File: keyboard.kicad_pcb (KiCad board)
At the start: 2 copper layers, 285 x 94.6 mm, 398 parts, among them IC1 ATMEGA32U4, J1 MINI, J2 MICRO, P1 CONN_1, P10 CONN_1, P11 CONN_1, P12 CONN_1, P13 CONN_1, P14 CONN_1, P15 CONN_1, P16 CONN_1, P17 CONN_1, P18 CONN_1, P19 CONN_1, P2 CONN_1, P20 CONN_1, P21 CONN_1, P22 CONN_1, P23 CONN_1, P24 CONN_1, P25 CONN_1, P26 CONN_1, P27 CONN_1, P28 CONN_1, P29 CONN_1, P3 CONN_1, P30 CONN_1, P31 CONN_1, P32 CONN_1, P33 CONN_1, P34 CONN_1, P35 CONN_1, P36 CONN_1, P37 CONN_1, P38 CONN_1, P39 CONN_1, P4 CONN_1, P40 CONN_1, P41 CONN_1, P42 CONN_1, P5 CONN_1, P6 CONN_1, P7 CONN_1, P8 CONN_1, P9 CONN_1, Q1 MOSFET_P, X1 CRYSTAL

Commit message: 完成
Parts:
- removed D01, D02, D03, D04, D05, D06, D07, D08, D09: 1N4148, SM0805D
- removed DB10, DB101, DB102, DB11, DB14, DB15, DB151, DB16, DB17, DB19, DB2, DB21, DB22, DB23, DB24, DB26, DB27, DB28, DB29, DB30, DB301, DB302, DB31, DB32, DB33, DB34, DB36, DB37, DB38, DB39, DB4, DB41, DB42, DB43, DB44, DB46, DB47, DB48, DB49, DB4_1, DB5, DB50, DB51, DB52, DB53, DB54, DB55, DB551, DB56, DB57, DB58, DB59, DB5_1, DB6, DB61, DB62, DB63, DB66, DB661, DB67, DB68, DB681, DB682, DB69, DB7, DB9, DF10, DF11, DF20, DF201, DF21, DF211, DF22, DF221, DF23, DF231, DF232, DF3, DW1, DW2, DW3, DW4: LED, MX1A-led
- removed FID (x2): FIDUCIAL, FIDUCIAL
- removed IC1: ATMEGA32U4, TQFP44
- removed J2: MICRO, Connect:USB_Micro-B
- removed JP1, JP2, JP3, JP4, JP5, JP6: JUMPER, Resistors_SMD:R_0201
- removed MXWIRE (x9): VAL**, MX1A-wire
- removed P1, P10, P11, P12, P13, P14, P15, P16, P17, P18, P19, P20, P21, P22, P23, P24, P25, P26, P27, P28, P29, P30, P31, P32, P33, P34, P35, P36, P37, P38, P39, P4, P40, P41, P42, P5, P6, P7, P8, P9: CONN_1, pad
- removed Q1: MOSFET_P, TO_SOT_Packages_SMD:SOT-23
- removed R11, R12, R13, R14, R15, R16, R17, R18, R19, R20, R21, R22, R23, R24, R25, R26, R27, R28, R29, R30, R31, R32, R33, R34, R35, R36, R37, R38, R39, R40, R41, R42, R43, R44, R45, R46, R47, R48, R49, R50, R51, R52, R53, R54, R55, R56, R57, R58, R59, R60, R61, R62, R63, R64, RL1, RL2, RL3, RL4, RL5: 300, Resistors_SMD:R_0805
- removed R65: 10k, Resistors_SMD:R_0805
- removed S0: DTSM-6, KSEM31GLFS
- removed S01, S02, S03, S04, S05, S0512, S06, S07, S08, S09: MX1A, MX1A-b
- removed X1: CRYSTAL, Crystals:Crystal_HC49-U_Vertical
- added D1: 1N4148, Diode_SMD:D_0805_2012Metric, B.Cu at (67.5, 81.5)
- added D2: 1N4148, Diode_SMD:D_0805_2012Metric, B.Cu at (68.6, 98.0)
- added D20: LED, MX1A:MX1A-led, F.Cu at (90.5, 73.8)
- added D25: LED, MX1A:MX1A-led, F.Cu at (109.5, 73.8)
- added D3: 1N4148, Diode_SMD:D_0805_2012Metric, B.Cu at (67.9, 117.0)
- added D35: LED, MX1A:MX1A-led, F.Cu at (128.6, 73.8)
- added D4: 1N4148, Diode_SMD:D_0805_2012Metric, B.Cu at (68.2, 136.1)
- added D40: LED, MX1A:MX1A-led, F.Cu at (147.6, 73.8)
- added D45: LED, MX1A:MX1A-led, F.Cu at (166.7, 73.8)
- added D5: 1N4148, Diode_SMD:D_0805_2012Metric, B.Cu at (70.1, 152.7)
- added D6: 1N4148, Diode_SMD:D_0805_2012Metric, B.Cu at (87.0, 81.8)
- added D7: 1N4148, Diode_SMD:D_0805_2012Metric, B.Cu at (94.9, 95.6)
- added D8: 1N4148, Diode_SMD:D_0805_2012Metric, B.Cu at (101.2, 119.9)
- added D9: 1N4148, Diode_SMD:D_0805_2012Metric, B.Cu at (91.4, 133.6)
- added G***: LOGO, custom:Cirno_Ice, B.Cu at (135.9, 149.6)
- added K1: Jumper_NO_Small, Resistor_SMD:R_0805_2012Metric, B.Cu at (157.7, 140.0)
- added S1: MX1A, MX1A:MX1A-simple, F.Cu at (71.4, 73.8)
- added S2: MX1A, MX1A:MX1A-simple, F.Cu at (76.2, 92.9)
- added S3: MX1A, MX1A:MX1A-simple, F.Cu at (73.8, 111.9)
- added S4: MX1A, MX1A:MX1A-simple, F.Cu at (83.3, 131.0)
- added S5: MX1A, MX1A:MX1A-simple, F.Cu at (73.8, 150.0)
- added S512: MX1A, MX1A:MX1A-simple, F.Cu at (76.2, 150.0)
- added S6: MX1A, MX1A:MX1A-simple, F.Cu at (90.5, 73.8)
- added S7: MX1A, MX1A:MX1A-simple, F.Cu at (100.0, 92.9)
- added S8: MX1A, MX1A:MX1A-simple, F.Cu at (104.8, 111.9)
- added S9: MX1A, MX1A:MX1A-simple, F.Cu at (95.2, 131.0)
- added U1: nrf51822-02, custom:nRF51822-02, B.Cu at (211.2, 158.5)
- added U2: TP4057, Package_TO_SOT_SMD:SOT-23-6, B.Cu at (155.6, 152.9)
- added U3: RT9193, Package_TO_SOT_SMD:SOT-23-5, B.Cu at (158.9, 156.7)
- added U4: CH554T, Package_SO:SSOP-20_4.4x6.5mm_P0.65mm, B.Cu at (163.3, 145.8)
- C1: value 22p -> 22nF; footprint SM0805 -> Capacitor_SMD:C_0805_2012Metric
- C2: value 22p -> 1uF; footprint SM0805 -> Capacitor_SMD:C_0805_2012Metric
- C3: value 1u -> 1uF; footprint SM0805 -> Capacitor_SMD:C_0805_2012Metric
- C4: value 100n -> 1uF; footprint SM0805 -> Capacitor_SMD:C_0805_2012Metric
- C5: value 100n -> 22uF; footprint SM0805 -> Capacitor_SMD:C_0805_2012Metric
- C6, C7: value 100n -> 0.1uF; footprint SM0805 -> Capacitor_SMD:C_0805_2012Metric
- C8: value 1u -> 47pF; footprint SM0805 -> Capacitor_SMD:C_0805_2012Metric
- D10, D11, D12, D13, D14, D15, D16, D17, D18, D19, D21, D22, D23, D24, D26, D27, D28, D29, D30, D31, D32, D33, D34, D36, D37, D38, D39, D41, D42, D43, D44, D46, D47, D48, D49, D50, D51, D52, D53, D54, D55, D56, D57, D58, D59, D60, D61, D62, D63, D64, D65, D66, D67, D68, D69, D70: footprint SM0805D -> Diode_SMD:D_0805_2012Metric
- DC1, DC2: footprint MX1A-led -> MX1A:MX1A-led
- DC3: footprint MX1A-ledlock -> MX1A:MX1A-led
- J1: value MINI -> USB_OTG; footprint 67503 -> custom:USB_Micro-B_lowp
- P2: value CONN_1 -> BATT; footprint pad -> Connector_PinHeader_2.54mm:PinHeader_1x02_P2.54mm_Vertical; moved to B.Cu
- P3: value CONN_1 -> SWD; footprint pad -> Connector_PinSocket_2.54mm:PinSocket_1x04_P2.54mm_Vertical; moved to B.Cu
- R1: value 22 -> 1.5K; footprint SM0805 -> Resistor_SMD:R_0805_2012Metric
- R10: value 300 -> 20K; footprint Resistors_SMD:R_0805 -> Resistor_SMD:R_0805_2012Metric
- R2: value 22 -> R; footprint SM0805 -> Resistor_SMD:R_0805_2012Metric
- R3, R5: value 10k -> R; footprint SM0805 -> Resistor_SMD:R_0805_2012Metric
- R4: footprint Resistors_SMD:R_0805 -> Resistor_SMD:R_0805_2012Metric
- R6: value 300 -> 10M; footprint Resistors_SMD:R_0805 -> Resistor_SMD:R_0805_2012Metric
- R7, R9: value 300 -> R; footprint Resistors_SMD:R_0805 -> Resistor_SMD:R_0805_2012Metric
- R8: value 300 -> 2.2M; footprint Resistors_SMD:R_0805 -> Resistor_SMD:R_0805_2012Metric
- S031, S041, S10, S101, S102, S11, S12, S13, S14, S15, S151, S16, S17, S18, S19, S21, S22, S23, S24, S26, S27, S28, S29, S30, S301, S302, S31, S32, S33, S34, S36, S37, S38, S39, S41, S42, S43, S44, S46, S47, S48, S49, S50, S51, S52, S53, S54, S55, S552, S56, S57, S58, S59, S60, S601, S602, S62, S63, S64, S641, S65, S6512, S66, S661, S67, S68, S681, S682, S69, S691, S692, S70, S7012: footprint MX1A-b -> MX1A:MX1A-simple
- moved C8 105.0 mm to (160.0, 140.0), turned to 270 degrees
- moved R1 104.7 mm to (155.6, 149.9), turned to 0 degrees
- moved R9 100.8 mm to (172.7, 71.0)
- moved R6 87.6 mm to (163.1, 153.7), turned to 0 degrees
- moved R10 86.4 mm to (162.3, 140.0), turned to 270 degrees
- moved R3 85.7 mm to (114.0, 70.2), turned to 0 degrees
- moved R5 83.8 mm to (134.0, 70.1), turned to 0 degrees
- moved R8 72.9 mm to (166.8, 151.5)
- moved P2 64.5 mm to (155.3, 156.8), turned to 90 degrees
- moved R7 58.2 mm to (152.7, 70.6)
- moved R4 33.5 mm to (83.6, 106.8), turned to 180 degrees
- moved P3 30.7 mm to (247.8, 153.3)
- moved C5 17.2 mm to (166.8, 153.7), turned to 0 degrees
- moved R2 15.6 mm to (96.2, 71.0), turned to 0 degrees
- moved C7 15.1 mm to (156.5, 146.8), turned to 270 degrees
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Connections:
- net /Matrix/col10 renamed /col10
- net /Matrix/col11 renamed /col11
- net /Matrix/col12 renamed /col12
- net /Matrix/col13 renamed /col13
- net /Matrix/col14 renamed /col14
- net /Matrix/col3 renamed /col3
- net /Matrix/col4 renamed /col4
- net /Matrix/col5 renamed /col5
- net /Matrix/col6 renamed /col6
- net /Matrix/col7 renamed /col7
- net /Matrix/col9 renamed /col9
- net /Matrix/row1 renamed /row1
- net /Matrix/row2 renamed /row2
- net /Matrix/row3 renamed /row3
- net /Matrix/row4 renamed /row4
- net /Matrix/row5 renamed /row5
- C2 pad 1: Net-(C2-Pad1) -> VCC
- C3 pad 1: Net-(C3-Pad1) -> BATT
- C4 pad 1: VCC -> 3V3
- C5 pad 1: VCC -> ADC1
- C6 pad 1: VCC -> V33
- C8 pad 1: VCC -> Net-(C8-Pad1)
- D10 pad 1: /Matrix/col2 -> /col2
- D36 pad 1: /Matrix/col8 -> /col8
- D37 pad 1: /Matrix/col8 -> /col8
- D38 pad 1: /Matrix/col8 -> /col8
- D39 pad 1: /Matrix/col8 -> /col8
- DC1 pad 1: VCC -> Net-(DC1-Pad1)
- DC1 pad 2: Net-(DC1-Pad2) -> GND
- DC2 pad 1: VCC -> Net-(DC1-Pad1)
- DC2 pad 2: Net-(DC1-Pad2) -> GND
- DC3 pad 1: VCC -> Net-(DC1-Pad1)
- J1 pad 2: Net-(J1-Pad2) -> UD_N
- J1 pad 3: Net-(J1-Pad3) -> UD_P
- J1 pad 4: (no net) -> Net-(J1-Pad4)
- P2 pad 1: VCC -> BATT
- P3 pad 1: /Matrix/col8 -> 3V3
- R1 pad 2: Net-(J1-Pad2) -> GND
- R10 pad 1: Net-(DB11-Pad1) -> Net-(C8-Pad1)
- R10 pad 2: /Leds/lcol3 -> UD_P
- R2 pad 2: Net-(J1-Pad3) -> /led1
- R3 pad 2: GND -> /led2
- R4 pad 1: Net-(DC1-Pad2) -> /caps_led
- R4 pad 2: /Matrix/CAPS_LED -> Net-(DC1-Pad1)
- R5 pad 1: VCC -> Net-(D35-Pad2)
- R5 pad 2: /~RES~ -> /led3
- R6 pad 1: Net-(DB7-Pad1) -> BATT
- R6 pad 2: /Leds/lcol2 -> ADC1
- R7 pad 2: /Leds/lcol2 -> /led4
- R8 pad 1: Net-(DB9-Pad1) -> ADC1
- R8 pad 2: /Leds/lcol2 -> GND
- R9 pad 2: /Leds/lcol2 -> /led5
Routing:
- net /Leds/lrow5: track 597.7 -> 0.00 mm, vias 18 -> 0
- net GND: track 546.1 -> 102.2 mm, vias 34 -> 11
- net /Leds/lrow1: track 385.6 -> 0.00 mm, vias 3 -> 0
- net /Leds/lrow4: track 377.2 -> 0.00 mm, vias 7 -> 0
- net VCC: track 488.3 -> 165.0 mm, vias 10 -> 4
- net /Leds/lrow2: track 322.1 -> 0.00 mm, vias 6 -> 0
- net /Leds/lrow3: track 297.3 -> 0.00 mm, vias 1 -> 0
- net /GPIO2: track 252.2 -> 0.00 mm, vias 6 -> 0
- net /Leds/lcol10: track 242.3 -> 0.00 mm, vias 7 -> 0
- net /GPIO1: track 240.9 -> 0.00 mm, vias 6 -> 0
- net /Leds/lcol14: track 238.1 -> 0.00 mm, vias 1 -> 0
- net /col1: track 0.00 -> 231.5 mm, vias 0 -> 2
- net /~RES~: track 226.3 -> 0.00 mm, vias 9 -> 0
- net /col2: track 0.00 -> 217.6 mm, vias 0 -> 2
- net /GPIO3: track 213.7 -> 0.00 mm, vias 5 -> 0
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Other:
- outline, holes or cut-outs redrawn
- net class DATA added: clearance 0.2032, trace_width 0.3048, via_dia 1, via_drill 0.4
- net class POWER: trace_width 0.508 -> 0.4064
- board text added: "Cirno id: 52846813"
- board text added: "Lot60-BLE Rev.A ©2018 Lotlab"
- board text removed: "0"
- board text removed: "1"
- board text removed: "2"
- board text removed: "3"
- board text removed: "CAPS"
- board text removed: "GPIO"
- board text removed: "ISP"
- board text removed: "JP2"
- board text removed: "JP3"
- board text removed: "JP4"
- board text removed: "MISO SCK RST"
- board text removed: "R1"
- board text removed: "R2"
- board text removed: "R3"
- board text removed: "R4"
- board text removed: "R5"
- board text removed: "Rev. L v1.01c Modify by Lotlab."
- board text removed: "VCC MOSI GND"
- board text removed: "expansion module"

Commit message: 细节修正
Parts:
- moved D69 5.64 mm to (323.4, 136.5)
- moved D32 5.40 mm to (191.8, 100.9)
- moved G*** 0.09 mm to (135.8, 149.5)
- renumbered C6 to C1, C7 to C2, C8 to C3, C2 to C4, C3 to C5, C4 to C6, C5 to C7, C1 to C8, D20 to LED1, D25 to LED2, D35 to LED3, D40 to LED4, D45 to LED5, P3 to P1, R10 to R1, R1 to R2, R6 to R3, R8 to R4, R4 to RL0, R2 to RL1, R3 to RL2, R5 to RL3, R7 to RL4, R9 to RL5, U4 to U2, U2 to U3, U3 to U4
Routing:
- net /col14: track 175.5 -> 187.4 mm
- net /row2: track 334.6 -> 323.0 mm
- net Net-(D64-Pad2): track 45.2 -> 35.9 mm
- net Net-(D69-Pad2): track 30.0 -> 39.2 mm
- net /row1: track 361.6 -> 368.0 mm, vias 0 -> 2
- net /led3: track 155.7 -> 161.9 mm
- net GND: track 102.2 -> 105.6 mm
- net /led5: track 127.6 -> 130.3 mm
- net /led4: track 138.3 -> 139.6 mm
- net ADC1: track 59.9 -> 60.8 mm
- net /caps_led: track 185.1 -> 185.9 mm
- net /row3: track 332.2 -> 331.5 mm
- net /col3: track 198.1 -> 198.8 mm
- net /col8: track 95.5 -> 94.9 mm
- net /col1: track 231.5 -> 231.0 mm
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
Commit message: 元件丢正面
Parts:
- C1, C2, C4, C5, C6, C8, D1, D10, D11, D12, D13, D14, D15, D16, D17, D18, D19, D2, D21, D22, D23, D24, D26, D27, D28, D29, D3, D30, D31, D32, D33, D34, D36, D37, D38, D39, D4, D41, D42, D43, D44, D46, D47, D48, D49, D5, D50, D51, D52, D53, D54, D55, D56, D57, D58, D59, D6, D60, D61, D62, D63, D64, D65, D66, D67, D68, D69, D7, D70, D8, D9, J1, P1, P2, R1, R2, R3, R4, RL0, RL1, RL2, RL3, RL4, RL5, U1, U2, U3, U4: moved to F.Cu
- C3: value 47pF -> NC/47pF; moved to F.Cu
- C7: value 22uF -> 10nF; moved to F.Cu
- moved P1 99.9 mm to (147.8, 153.0), turned to 180 degrees
- moved G*** 90.1 mm to (225.9, 149.1)
- moved P2 59.5 mm to (212.5, 140.5), turned to 270 degrees
- moved U4 55.7 mm to (214.5, 154.7), turned to 180 degrees
- moved C8 52.3 mm to (214.5, 152.0), turned to 0 degrees
- moved R3 52.0 mm to (214.5, 145.9), turned to 180 degrees
- moved C5 52.0 mm to (214.6, 143.9), turned to 180 degrees
- moved C6 48.4 mm to (214.5, 157.3), turned to 0 degrees
- moved C7 47.9 mm to (214.5, 150.0)
- moved R4 47.9 mm to (214.5, 148.0)
- moved C1 33.3 mm to (137.5, 154.4), turned to 180 degrees
- moved U1 32.4 mm to (178.8, 158.1)
- moved R1 31.8 mm to (134.0, 154.4), turned to 0 degrees
- moved C3 30.8 mm to (134.0, 156.4), turned to 0 degrees
- moved U2 27.8 mm to (135.7, 149.2), turned to 270 degrees
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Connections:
- K1 pad 2: VCC -> V33
- U1 pad 10: /col3 -> /col7
- U1 pad 12: /col4 -> /led5
- U1 pad 13: /col5 -> /col6
- U1 pad 14: /col6 -> /led4
- U1 pad 15: /col7 -> /col5
- U1 pad 16: /col8 -> /led3
- U1 pad 17: /col9 -> /col4
- U1 pad 18: /col10 -> /led2
- U1 pad 19: /col11 -> /col3
- U1 pad 20: /col12 -> /led1
- U1 pad 23: /col13 -> /col2
- U1 pad 24: /col14 -> /caps_led
- U1 pad 25: Net-(U1-Pad25) -> /col1
- U1 pad 3: /row5 -> /col14
- U1 pad 32: /led5 -> TXD
- U1 pad 33: /led4 -> RXD
- U1 pad 34: /led3 -> Net-(U1-Pad34)
- U1 pad 35: /led2 -> /row1
- U1 pad 36: /led1 -> /row2
- U1 pad 37: /caps_led -> /row3
- U1 pad 38: Net-(U1-Pad38) -> /row4
- U1 pad 39: TXD -> /row5
- U1 pad 4: /row4 -> /col13
- U1 pad 40: RXD -> Net-(U1-Pad40)
- U1 pad 5: /row3 -> /col12
- U1 pad 6: /row2 -> /col11
- U1 pad 7: /row1 -> /col10
- U1 pad 8: /col1 -> /col9
- U1 pad 9: /col2 -> /col8
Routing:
- net BATT: track 15.9 -> 102.8 mm, vias 0 -> 3
- net /caps_led: track 185.9 -> 99.5 mm
- net /col6: track 158.6 -> 79.4 mm, vias 2 -> 0
- net /led3: track 161.9 -> 87.0 mm
- net /row1: track 368.0 -> 438.6 mm, vias 2 -> 4
- net /led2: track 181.2 -> 111.7 mm
- net /led1: track 198.1 -> 128.8 mm
- net /col2: track 218.0 -> 157.2 mm
- net /col3: track 198.8 -> 143.2 mm
- net /col13: track 158.1 -> 213.6 mm
- net /col1: track 231.0 -> 176.0 mm
- net /col4: track 162.8 -> 108.9 mm
- net /col5: track 145.3 -> 92.2 mm, vias 2 -> 0
- net /led5: track 130.3 -> 77.9 mm, vias 2 -> 0
- net /led4: track 139.6 -> 88.2 mm
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
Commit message: 修改
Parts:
- removed C8: 22nF, Capacitor_SMD:C_0805_2012Metric
- MXST (x15): footprint MXST -> MX1A:MXST
- U4: value RT9193 -> XC6206P30; footprint Package_TO_SOT_SMD:SOT-23-5 -> Package_TO_SOT_SMD:SOT-23
- moved U4 1.91 mm to (214.5, 152.8), turned to 0 degrees
- moved C6 1.72 mm to (214.5, 155.6)
- moved G*** 1.27 mm to (225.9, 150.4)
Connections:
- U4 pad 1: BATT -> GND
- U4 pad 2: GND -> 3V3
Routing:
- net GND: track 72.8 -> 83.6 mm
- net BATT: track 102.8 -> 97.9 mm
- net Net-(C8-Pad1): track 1.78 -> 0.00 mm
- net /col1: track 176.0 -> 177.6 mm
- net DIO: track 19.7 -> 20.7 mm
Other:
- board text added: "id: 52846813"
- board text removed: "Cirno id: 52846813"

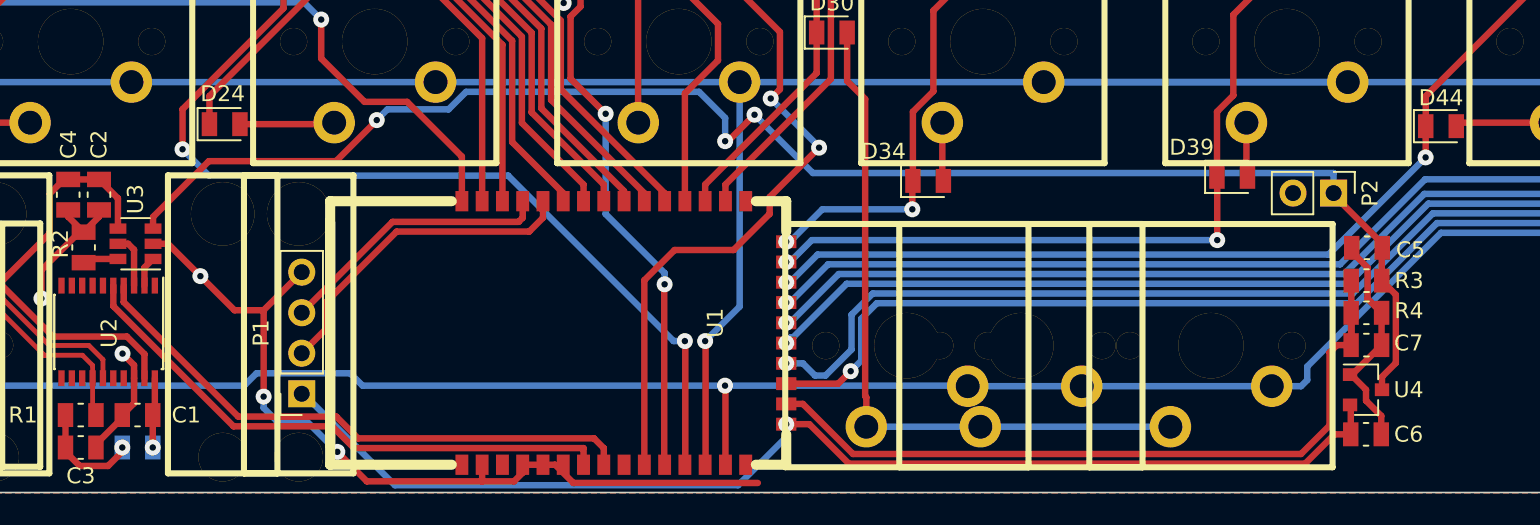
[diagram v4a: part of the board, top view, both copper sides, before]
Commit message: 修正几个问题
修正ADC接口不正确的问题
增加防反冲二极管
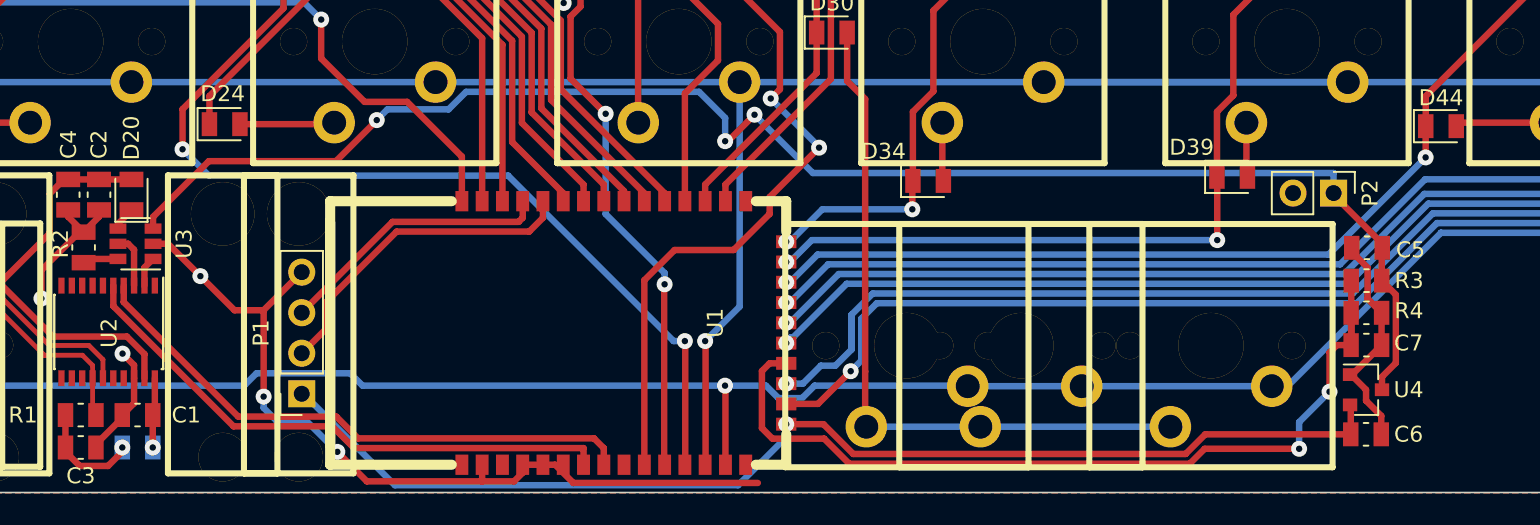
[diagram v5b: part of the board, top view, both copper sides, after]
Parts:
- added D20: SS14, Diode_SMD:D_0805_2012Metric, F.Cu at (137.2, 140.6)
- R1: value 20K -> 10K
- R2: value 1.5K -> 4.7K
- renumbered S031 to S3001, S041 to S4001
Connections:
- U1 pad 2: ADC1 -> /col14
- U1 pad 3: /col14 -> /col13
- U1 pad 4: /col13 -> ADC1
- U3 pad 4: VCC -> Net-(D20-Pad1)
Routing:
- net ADC1: track 48.3 -> 54.9 mm, vias 0 -> 2
- net /col13: track 213.6 -> 215.7 mm
- net VCC: track 131.2 -> 129.6 mm
- net Net-(D20-Pad1): track 0.00 -> 1.49 mm
- net /col14: track 233.7 -> 234.3 mm
- net 3V3: track 73.8 -> 73.3 mm
